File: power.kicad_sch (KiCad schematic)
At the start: 26 parts, among them J1 Barrel_Jack, U1 AP64501, U9 TPS79933

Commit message: geographical reannotate
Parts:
- renumbered C25 to C1, C1 to C11, C4 to C13, C22 to C19, C19 to C21, C23 to C22, C21 to C24, C9 to C3, C3 to C4, C11 to C5, C2 to C6, C10 to C7, D2 to D10, D3 to D5, D19 to D6, D1 to D9, J1 to J3, JP2 to JP4, R31 to R22, R3 to R4, R1 to R8, R2 to R9, U9 to U4, U1 to U5
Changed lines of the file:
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@@
   (symbol (lib_id "Jumper:SolderJumper_2_Open") (at 247.015 131.445 90) (unit 1)
     (in_bom yes) (on_board yes)
-    (property "Reference" "JP2" (id 0) (at 249.1487 130.2956 90)
+    (property "Reference" "JP4" (id 0) (at 249.1487 130.2956 90)
       (effects (font (size 1.27 1.27)) (justify right))
     )
@@
   (symbol (lib_id "Device:R") (at 113.03 187.96 0) (unit 1)
     (in_bom yes) (on_board yes) (fields_autoplaced)
-    (property "Reference" "R31" (id 0) (at 115.57 186.6899 0)
+    (property "Reference" "R22" (id 0) (at 115.57 186.6899 0)
       (effects (font (size 1.27 1.27)) (justify left))
     )
@@
   (symbol (lib_id "Device:R") (at 194.31 125.095 0) (unit 1)
     (in_bom yes) (on_board yes)
-    (property "Reference" "R2" (id 0) (at 196.0881 123.9456 0)
+    (property "Reference" "R9" (id 0) (at 196.0881 123.9456 0)
       (effects (font (size 1.27 1.27)) (justify left))
     )
@@
   (symbol (lib_id "Device:R") (at 194.31 135.255 0) (unit 1)
     (in_bom yes) (on_board yes)
-    (property "Reference" "R1" (id 0) (at 196.0881 134.1056 0)
+    (property "Reference" "R8" (id 0) (at 196.0881 134.1056 0)
       (effects (font (size 1.27 1.27)) (justify left))
     )
@@
   (symbol (lib_id "Device:R") (at 238.125 127.635 0) (unit 1)
     (in_bom yes) (on_board yes)
-    (property "Reference" "R3" (id 0) (at 239.9031 126.4856 0)
+    (property "Reference" "R4" (id 0) (at 239.9031 126.4856 0)
       (effects (font (size 1.27 1.27)) (justify left))
     )
@@
   (symbol (lib_id "symbols:Diode") (at 62.23 30.48 180) (unit 1)
     (in_bom yes) (on_board yes)
-    (property "Reference" "D1" (id 0) (at 62.23 27.324 0))
+    (property "Reference" "D9" (id 0) (at 62.23 27.324 0))
     (property "Value" "Diode" (id 1) (at 73.66 38.1 0)
       (effects (font (size 1.27 1.27)) hide)
@@
   (symbol (lib_id "symbols:Diode") (at 62.23 36.83 180) (unit 1)
     (in_bom yes) (on_board yes)
-    (property "Reference" "D2" (id 0) (at 62.23 33.674 0))
+    (property "Reference" "D10" (id 0) (at 62.23 33.674 0))
     (property "Value" "Diode" (id 1) (at 73.66 44.45 0)
       (effects (font (size 1.27 1.27)) hide)
@@
   (symbol (lib_id "symbols:Diode") (at 62.23 43.18 180) (unit 1)
     (in_bom yes) (on_board yes)
-    (property "Reference" "D3" (id 0) (at 62.23 40.024 0))
+    (property "Reference" "D5" (id 0) (at 62.23 40.024 0))
     (property "Value" "Diode" (id 1) (at 73.66 50.8 0)
       (effects (font (size 1.27 1.27)) hide)
@@
   (symbol (lib_id "ecafe-racer:LED_Green") (at 113.03 180.34 90) (unit 1)
     (in_bom yes) (on_board yes) (fields_autoplaced)
-    (property "Reference" "D19" (id 0) (at 116.84 179.2604 90)
+    (property "Reference" "D6" (id 0) (at 116.84 179.2604 90)
       (effects (font (size 1.27 1.27)) (justify right))
     )
@@
   (symbol (lib_id "Device:C") (at 62.23 116.84 0) (unit 1)
     (in_bom yes) (on_board yes) (fields_autoplaced)
-    (property "Reference" "C9" (id 0) (at 65.405 115.5699 0)
+    (property "Reference" "C3" (id 0) (at 65.405 115.5699 0)
       (effects (font (size 1.27 1.27)) (justify left))
     )
@@
   (symbol (lib_id "Device:C") (at 79.375 107.95 0) (unit 1)
     (in_bom yes) (on_board yes) (fields_autoplaced)
-    (property "Reference" "C10" (id 0) (at 82.55 106.6799 0)
+    (property "Reference" "C7" (id 0) (at 82.55 106.6799 0)
       (effects (font (size 1.27 1.27)) (justify left))
     )
@@
   (symbol (lib_id "Device:C") (at 88.9 107.95 0) (unit 1)
     (in_bom yes) (on_board yes) (fields_autoplaced)
-    (property "Reference" "C11" (id 0) (at 92.075 106.6799 0)
+    (property "Reference" "C5" (id 0) (at 92.075 106.6799 0)
       (effects (font (size 1.27 1.27)) (justify left))
     )
@@
   (symbol (lib_id "symbols:CAP-CERAMIC-10uF") (at 93.98 50.165 0) (unit 1)
     (in_bom yes) (on_board yes)
-    (property "Reference" "C3" (id 0) (at 96.9011 49.0156 0)
+    (property "Reference" "C4" (id 0) (at 96.9011 49.0156 0)
       (effects (font (size 1.27 1.27)) (justify left))
     )
@@
   (symbol (lib_id "Device:C") (at 105.41 50.165 0) (unit 1)
     (in_bom yes) (on_board yes)
-    (property "Reference" "C1" (id 0) (at 107.0611 52.8256 0)
+    (property "Reference" "C11" (id 0) (at 107.0611 52.8256 0)
       (effects (font (size 1.27 1.27)) (justify left))
     )
@@
   (symbol (lib_id "symbols:100uF") (at 109.22 107.95 0) (unit 1)
     (in_bom yes) (on_board yes)
-    (property "Reference" "C25" (id 0) (at 112.1411 106.8006 0)
+    (property "Reference" "C1" (id 0) (at 112.1411 106.8006 0)
       (effects (font (size 1.27 1.27)) (justify left))
     )
@@
   (symbol (lib_id "Device:C") (at 135.89 38.735 90) (unit 1)
     (in_bom yes) (on_board yes)
-    (property "Reference" "C23" (id 0) (at 135.89 32.3658 90))
+    (property "Reference" "C22" (id 0) (at 135.89 32.3658 90))
     (property "Value" "C" (id 1) (at 135.89 34.6645 90))
     (property "Footprint" "Capacitor_SMD:C_0805_2012Metric" (id 2) (at 139.7 37.7698 0)
@@
   (symbol (lib_id "symbols:100uF") (at 158.75 48.895 0) (unit 1)
     (in_bom yes) (on_board yes)
-    (property "Reference" "C2" (id 0) (at 161.6711 47.7456 0)
+    (property "Reference" "C6" (id 0) (at 161.6711 47.7456 0)
       (effects (font (size 1.27 1.27)) (justify left))
     )
@@
   (symbol (lib_id "symbols:CAP-CERAMIC-10uF") (at 171.45 48.895 0) (unit 1)
     (in_bom yes) (on_board yes)
-    (property "Reference" "C22" (id 0) (at 174.3711 47.7456 0)
+    (property "Reference" "C19" (id 0) (at 174.3711 47.7456 0)
       (effects (font (size 1.27 1.27)) (justify left))
     )
@@
   (symbol (lib_id "symbols:CAP-CERAMIC-10uF") (at 181.61 48.895 0) (unit 1)
     (in_bom yes) (on_board yes)
-    (property "Reference" "C19" (id 0) (at 184.5311 47.7456 0)
+    (property "Reference" "C21" (id 0) (at 184.5311 47.7456 0)
       (effects (font (size 1.27 1.27)) (justify left))
     )
@@
   (symbol (lib_id "Device:C") (at 185.42 125.095 0) (unit 1)
     (in_bom yes) (on_board yes)
-    (property "Reference" "C4" (id 0) (at 188.3411 123.9456 0)
+    (property "Reference" "C13" (id 0) (at 188.3411 123.9456 0)
       (effects (font (size 1.27 1.27)) (justify left))
     )
@@
   (symbol (lib_id "symbols:CAP-CERAMIC-10uF") (at 191.77 48.895 0) (unit 1)
     (in_bom yes) (on_board yes)
-    (property "Reference" "C21" (id 0) (at 194.6911 47.7456 0)
+    (property "Reference" "C24" (id 0) (at 194.6911 47.7456 0)
       (effects (font (size 1.27 1.27)) (justify left))
     )
@@
   (symbol (lib_id "symbols:Barrel_Jack") (at 36.83 45.72 0) (unit 1)
     (in_bom yes) (on_board yes)
-    (property "Reference" "J1" (id 0) (at 36.957 39.605 0))
+    (property "Reference" "J3" (id 0) (at 36.957 39.605 0))
     (property "Value" "Barrel_Jack" (id 1) (at 38.227 39.9985 0)
       (effects (font (size 1.27 1.27)) hide)
@@
   (symbol (lib_id "flip-pixel:TPS79933") (at 53.34 109.22 0) (unit 1)
     (in_bom yes) (on_board yes) (fields_autoplaced)
-    (property "Reference" "U9" (id 0) (at 53.34 98.425 0))
+    (property "Reference" "U4" (id 0) (at 53.34 98.425 0))
     (property "Value" "TPS79933" (id 1) (at 53.34 100.965 0))
     (property "Footprint" "Package_TO_SOT_SMD:SOT-23-5" (id 2) (at 57.15 101.6 0)
@@
   (symbol (lib_id "symbols:AP64501") (at 121.92 42.545 0) (unit 1)
     (in_bom yes) (on_board yes)
-    (property "Reference" "U1" (id 0) (at 122.555 32.1115 0))
+    (property "Reference" "U5" (id 0) (at 122.555 32.1115 0))
     (property "Value" "AP64501" (id 1) (at 122.555 34.4102 0))
     (property "Footprint" "Package_SO:SOIC-8-1EP_3.9x4.9mm_P1.27mm_EP2.514x3.2mm" (id 2) (at 111.76 41.275 0)

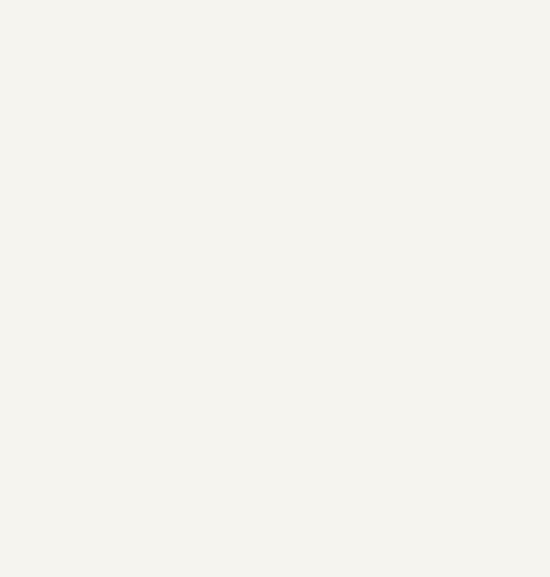
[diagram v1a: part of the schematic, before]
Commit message: added test points and cleaned up silk screen
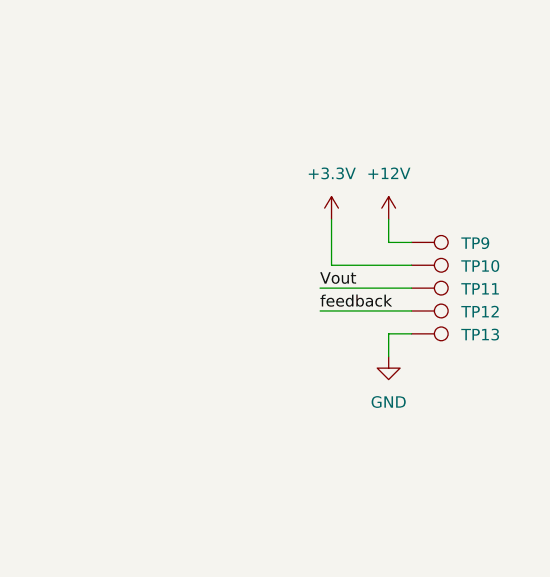
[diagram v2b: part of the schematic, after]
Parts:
- added TP10, TP11, TP12, TP13, TP9: TestPoint, TestPoint:TestPoint_Pad_D1.5mm, symbol Connector:TestPoint
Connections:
- net +12V: now also TP9.1
- net +3V3: now also TP10.1
- net 5Vout: now also TP11.1
- net GND: now also TP13.1
- net feedback: now also TP12.1
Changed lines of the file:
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@@
+    (stroke (width 0) (type solid) (color 0 0 0 0))
+  )
+  (wire (pts (xy 234.95 74.93) (xy 245.11 74.93))
+    (stroke (width 0) (type solid) (color 0 0 0 0))
+  )
+  (wire (pts (xy 234.95 77.47) (xy 245.11 77.47))
+    (stroke (width 0) (type solid) (color 0 0 0 0))
+  )
+  (wire (pts (xy 236.22 67.31) (xy 236.22 72.39))
+    (stroke (width 0) (type solid) (color 0 0 0 0))
+  )
+  (wire (pts (xy 236.22 72.39) (xy 245.11 72.39))
     (stroke (width 0) (type solid) (color 0 0 0 0))
   )
@@
   )
   (wire (pts (xy 238.125 141.605) (xy 247.015 141.605))
+    (stroke (width 0) (type solid) (color 0 0 0 0))
+  )
+  (wire (pts (xy 242.57 67.31) (xy 242.57 69.85))
+    (stroke (width 0) (type solid) (color 0 0 0 0))
+  )
+  (wire (pts (xy 242.57 80.01) (xy 242.57 82.55))
+    (stroke (width 0) (type solid) (color 0 0 0 0))
+  )
+  (wire (pts (xy 245.11 69.85) (xy 242.57 69.85))
+    (stroke (width 0) (type solid) (color 0 0 0 0))
+  )
+  (wire (pts (xy 245.11 80.01) (xy 242.57 80.01))
     (stroke (width 0) (type solid) (color 0 0 0 0))
   )
@@
     (effects (font (size 1.27 1.27)) (justify right bottom))
   )
+  (label "Vout" (at 234.95 74.93 0)
+    (effects (font (size 1.27 1.27)) (justify left bottom))
+  )
+  (label "feedback" (at 234.95 77.47 0)
+    (effects (font (size 1.27 1.27)) (justify left bottom))
+  )
   (label "comp" (at 238.125 116.205 270)
     (effects (font (size 1.27 1.27)) (justify right bottom))
@@
     (pin "1")
   )
+  (symbol (lib_id "power:+3.3V") (at 236.22 67.31 0) (unit 1)
+    (in_bom yes) (on_board yes) (fields_autoplaced)
+    (property "Reference" "#PWR0152" (id 0) (at 236.22 71.12 0)
+      (effects (font (size 1.27 1.27)) hide)
+    )
+    (property "Value" "+3.3V" (id 1) (at 236.22 62.23 0))
+    (property "Footprint" "" (id 2) (at 236.22 67.31 0)
+      (effects (font (size 1.27 1.27)) hide)
+    )
+    (property "Datasheet" "" (id 3) (at 236.22 67.31 0)
+      (effects (font (size 1.27 1.27)) hide)
+    )
+    (pin "1")
+  )
+  (symbol (lib_id "power:+12V") (at 242.57 67.31 0) (unit 1)
+    (in_bom yes) (on_board yes) (fields_autoplaced)
+    (property "Reference" "#PWR0151" (id 0) (at 242.57 71.12 0)
+      (effects (font (size 1.27 1.27)) hide)
+    )
+    (property "Value" "+12V" (id 1) (at 242.57 62.23 0))
+    (property "Footprint" "" (id 2) (at 242.57 67.31 0)
+      (effects (font (size 1.27 1.27)) hide)
+    )
+    (property "Datasheet" "" (id 3) (at 242.57 67.31 0)
+      (effects (font (size 1.27 1.27)) hide)
+    )
+    (pin "1")
+  )
+  (symbol (lib_id "Connector:TestPoint") (at 245.11 69.85 270) (unit 1)
+    (in_bom yes) (on_board yes)
+    (property "Reference" "TP9" (id 0) (at 250.6409 69.9771 90)
+      (effects (font (size 1.27 1.27)) (justify left))
+    )
+    (property "Value" "TestPoint" (id 1) (at 245.802 71.247 0)
+      (effects (font (size 1.27 1.27)) (justify left) hide)
+    )
+    (property "Footprint" "TestPoint:TestPoint_Pad_D1.5mm" (id 2) (at 245.11 74.93 0)
+      (effects (font (size 1.27 1.27)) hide)
+    )
+    (property "Datasheet" "~" (id 3) (at 245.11 74.93 0)
+      (effects (font (size 1.27 1.27)) hide)
+    )
+    (pin "1")
+  )
+  (symbol (lib_id "Connector:TestPoint") (at 245.11 72.39 270) (unit 1)
+    (in_bom yes) (on_board yes)
+    (property "Reference" "TP10" (id 0) (at 250.6409 72.5171 90)
+      (effects (font (size 1.27 1.27)) (justify left))
+    )
+    (property "Value" "TestPoint" (id 1) (at 245.802 73.787 0)
+      (effects (font (size 1.27 1.27)) (justify left) hide)
+    )
+    (property "Footprint" "TestPoint:TestPoint_Pad_D1.5mm" (id 2) (at 245.11 77.47 0)
+      (effects (font (size 1.27 1.27)) hide)
+    )
+    (property "Datasheet" "~" (id 3) (at 245.11 77.47 0)
+      (effects (font (size 1.27 1.27)) hide)
+    )
+    (pin "1")
+  )
+  (symbol (lib_id "Connector:TestPoint") (at 245.11 74.93 270) (unit 1)
+    (in_bom yes) (on_board yes)
+    (property "Reference" "TP11" (id 0) (at 250.6409 75.0571 90)
+      (effects (font (size 1.27 1.27)) (justify left))
+    )
+    (property "Value" "TestPoint" (id 1) (at 245.802 76.327 0)
+      (effects (font (size 1.27 1.27)) (justify left) hide)
+    )
+    (property "Footprint" "TestPoint:TestPoint_Pad_D1.5mm" (id 2) (at 245.11 80.01 0)
+      (effects (font (size 1.27 1.27)) hide)
+    )
+    (property "Datasheet" "~" (id 3) (at 245.11 80.01 0)
+      (effects (font (size 1.27 1.27)) hide)
+    )
+    (pin "1")
+  )
+  (symbol (lib_id "Connector:TestPoint") (at 245.11 77.47 270) (unit 1)
+    (in_bom yes) (on_board yes)
+    (property "Reference" "TP12" (id 0) (at 250.6409 77.5971 90)
+      (effects (font (size 1.27 1.27)) (justify left))
+    )
+    (property "Value" "TestPoint" (id 1) (at 245.802 78.867 0)
+      (effects (font (size 1.27 1.27)) (justify left) hide)
+    )
+    (property "Footprint" "TestPoint:TestPoint_Pad_D1.5mm" (id 2) (at 245.11 82.55 0)
+      (effects (font (size 1.27 1.27)) hide)
+    )
+    (property "Datasheet" "~" (id 3) (at 245.11 82.55 0)
+      (effects (font (size 1.27 1.27)) hide)
+    )
+    (pin "1")
+  )
+  (symbol (lib_id "Connector:TestPoint") (at 245.11 80.01 270) (unit 1)
+    (in_bom yes) (on_board yes)
+    (property "Reference" "TP13" (id 0) (at 250.6409 80.1371 90)
+      (effects (font (size 1.27 1.27)) (justify left))
+    )
+    (property "Value" "TestPoint" (id 1) (at 245.802 81.407 0)
+      (effects (font (size 1.27 1.27)) (justify left) hide)
+    )
+    (property "Footprint" "TestPoint:TestPoint_Pad_D1.5mm" (id 2) (at 245.11 85.09 0)
+      (effects (font (size 1.27 1.27)) hide)
+    )
+    (property "Datasheet" "~" (id 3) (at 245.11 85.09 0)
+      (effects (font (size 1.27 1.27)) hide)
+    )
+    (pin "1")
+  )
   (symbol (lib_id "power:GND") (at 44.45 114.3 0) (unit 1)
     (in_bom yes) (on_board yes) (fields_autoplaced)
@@
       (effects (font (size 1.27 1.27)) hide)
     )
+    (pin "1")
+  )
+  (symbol (lib_id "power:GND") (at 242.57 82.55 0) (unit 1)
+    (in_bom yes) (on_board yes) (fields_autoplaced)
+    (property "Reference" "#PWR0150" (id 0) (at 242.57 88.9 0)
+      (effects (font (size 1.27 1.27)) hide)
+    )
+    (property "Value" "GND" (id 1) (at 242.57 87.63 0))
+    (property "Footprint" "" (id 2) (at 242.57 82.55 0)
+      (effects (font (size 1.27 1.27)) hide)
+    )
+    (property "Datasheet" "" (id 3) (at 242.57 82.55 0)
+      (effects (font (size 1.27 1.27)) hide)
+    )
